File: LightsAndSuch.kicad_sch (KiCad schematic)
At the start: 62 parts, among them J1 Conn_ARM_SWD_TagConnect_TC2030, Q1 AO3400A, Q2 AO3400A, Q3 AO3400A, U1 STM32F205RBTx, U2 MAX98357A, U3 TPS54202DDC, U4 TPS7A20xxxDQN, U5 CD4081BM, U6 LM555xM, U7 LM555xM

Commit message: more or less finished with power
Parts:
- removed U4: TPS7A20xxxDQN, Package_SON:Texas_X2SON-4_1x1mm_P0.65mm, symbol Regulator_Linear:TPS7A20xxxDQN
- added J2: VIN, Connector_Molex:Molex_Micro-Fit_3.0_43045-0200_2x01_P3.00mm_Horizontal, symbol Connector:Conn_01x02_Pin
- added J3: TSA, Connector_Molex:Molex_Micro-Fit_3.0_43045-0200_2x01_P3.00mm_Horizontal, symbol Connector:Conn_01x02_Pin
- added J4: BMS Fault, Connector_Molex:Molex_Micro-Fit_3.0_43045-0200_2x01_P3.00mm_Horizontal, symbol Connector:Conn_01x02_Pin
- added J5: Button, Connector_Molex:Molex_Micro-Fit_3.0_43045-0200_2x01_P3.00mm_Horizontal, symbol Connector:Conn_01x02_Pin
- added J6: IMD Fault, Connector_Molex:Molex_Micro-Fit_3.0_43045-0200_2x01_P3.00mm_Horizontal, symbol Connector:Conn_01x02_Pin
- added J7: Break, Connector_Molex:Molex_Micro-Fit_3.0_43045-0200_2x01_P3.00mm_Horizontal, symbol Connector:Conn_01x02_Pin
- added U4: PTPS7A20185PDQNR, PTPS7A20185PDQNR:DQN0004A-MFG, symbol PTPS7A20185PDQNR:PTPS7A20185PDQNR
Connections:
- net +12V: now also J2.2 (Pin_2)
- net +3.3V: now also U4.1 (OUT)
- net +5V: now also U4.3 (EN), U4.4 (IN)
- net BMS_Fault: now also J4.2 (Pin_2)
- net Break: now also J7.2 (Pin_2)
- net Button: now also J5.2 (Pin_2)
- net GND: now also J2.1 (Pin_1), J3.1 (Pin_1), J4.1 (Pin_1), J5.1 (Pin_1), J6.1 (Pin_1), J7.1 (Pin_1), U4.2 (GND), U4.5 (Thermal_Pad)
- net IMD_Fault: now also J6.2 (Pin_2)
- net TSA: now also J3.2 (Pin_2)
- net SW: now reaches Cboot1.2, L1.1, U3.2 (SW)
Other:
- note added: "Connectors"
- moved on the sheet: C7, C8

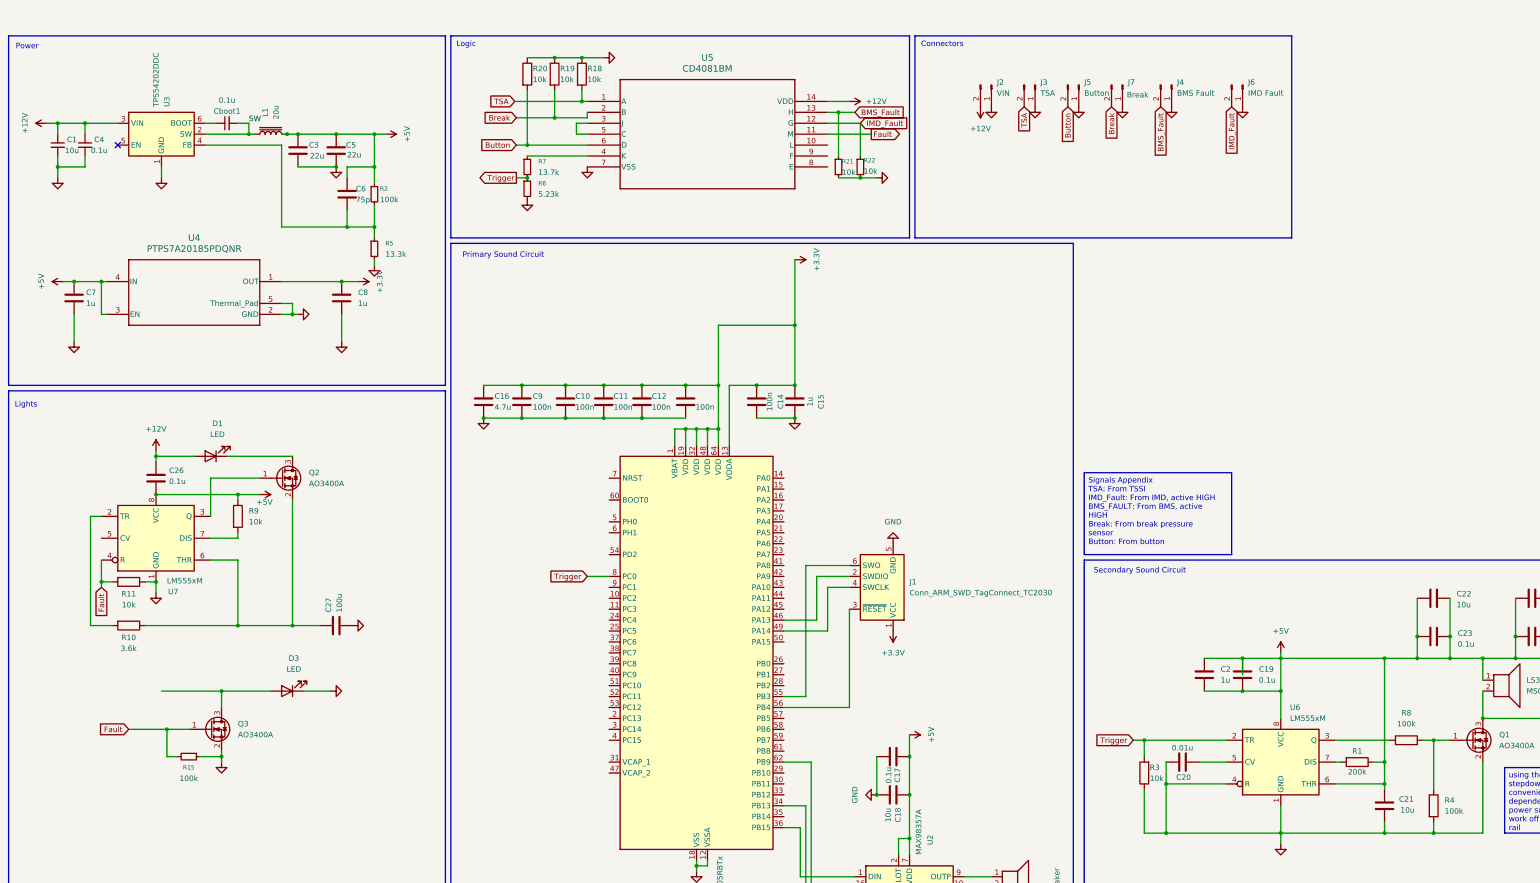
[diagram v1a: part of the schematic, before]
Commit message: finished power layout + inverted sig
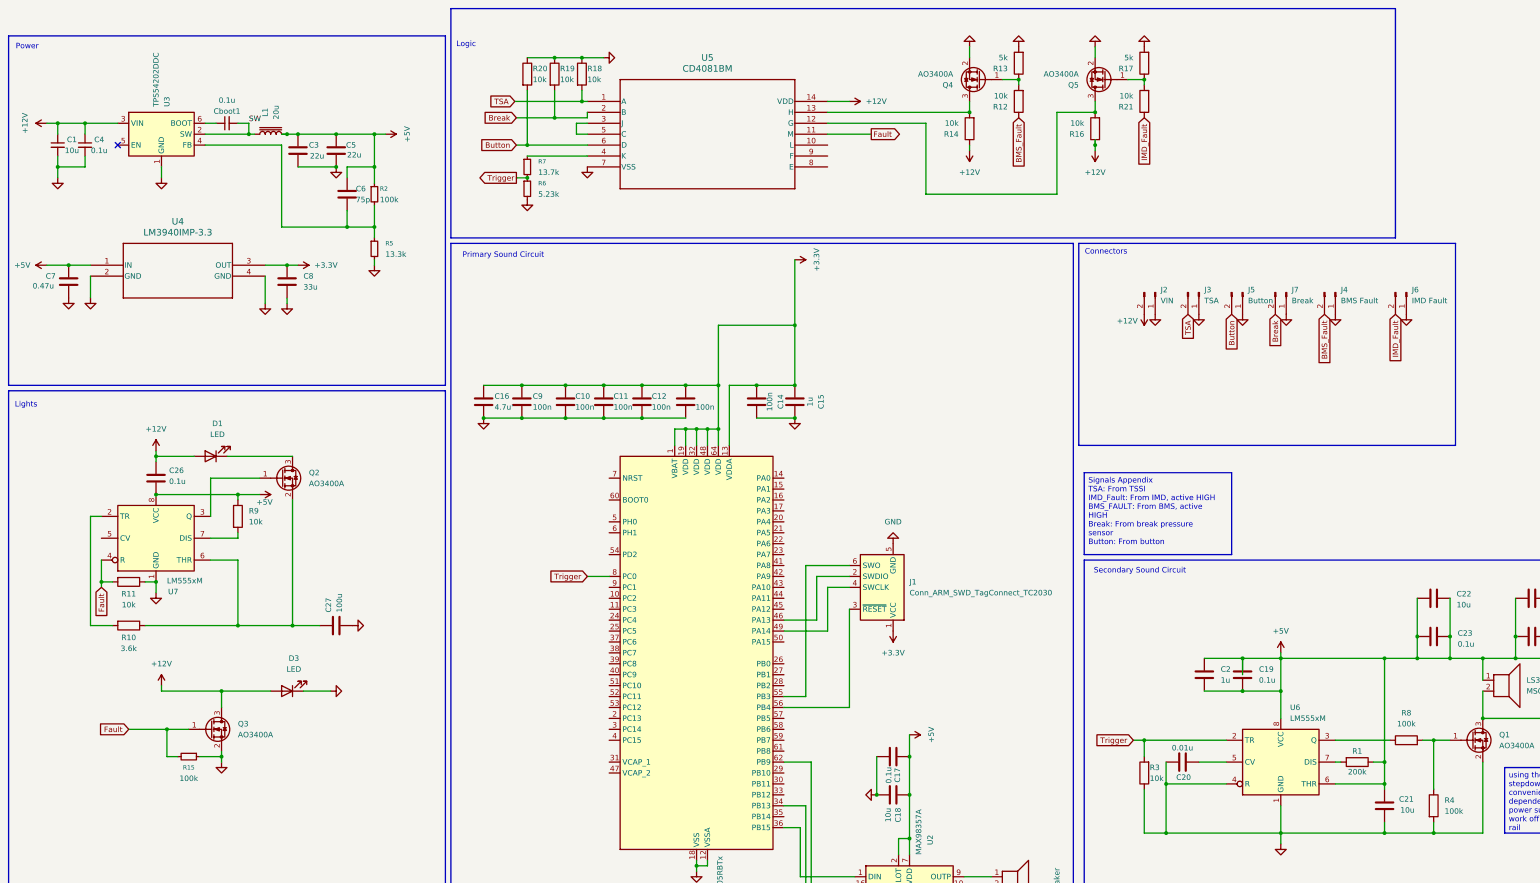
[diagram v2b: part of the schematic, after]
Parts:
- removed R21, R22: 10k, Resistor_SMD:R_0603_1608Metric, symbol Device:R_Small
- removed U4: PTPS7A20185PDQNR, PTPS7A20185PDQNR:DQN0004A-MFG, symbol PTPS7A20185PDQNR:PTPS7A20185PDQNR
- added Q4, Q5: AO3400A, Package_TO_SOT_SMD:SOT-23, symbol Transistor_FET:AO3400A
- added R12, R14, R16, R21: 10k, Resistor_SMD:R_0603_1608Metric, symbol Device:R
- added R13, R17: 5k, Resistor_SMD:R_0603_1608Metric, symbol Device:R
- added U4: LM3940IMP-3.3, LM3940:MP04A, symbol LM3940:LM3940IMP-3.3
- C7: value 1u -> 0.47u; footprint Capacitor_SMD:C_0201_0603Metric -> Capacitor_SMD:C_0603_1608Metric
- C8: value 1u -> 33u; footprint Capacitor_SMD:C_0201_0603Metric -> Capacitor_SMD:C_0603_1608Metric
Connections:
- net +12V: now also D3.2 (A), Q3.3 (D), R14.1, R16.1
- net +3.3V: now also U4.3 (OUT)
- net +5V: now also U4.1 (IN)
- net BMS_Fault: now also R12.1; no longer U5.13 (H)
- net GND: now also Q4.2 (S), Q5.2 (S), R13.2, R17.2, U4.2 (GND), U4.4 (GND)
- net IMD_Fault: now also R21.1; no longer U5.12 (G)
- new net: Q5.3 (D), R16.2, U5.12 (G)
- new net: Q5.1 (G), R17.1, R21.2
- new net: Q4.3 (D), R14.2, U5.13 (H)
- new net: Q4.1 (G), R12.2, R13.1
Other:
- moved on the sheet: J2, J3, J4, J5, J6, J7

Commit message: rp2040
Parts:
- removed J1: Conn_ARM_SWD_TagConnect_TC2030, Connector:Tag-Connect_TC2030-IDC-FP_2x03_P1.27mm_Vertical, symbol Connector:Conn_ARM_SWD_TagConnect_TC2030
- removed U1: STM32F205RBTx, Package_QFP:LQFP-64_10x10mm_P0.5mm, symbol MCU_ST_STM32F2:STM32F205RBTx
- added C28, C29, C30: C, Capacitor_SMD:C_0201_0603Metric, symbol Device:C
- added C31: 100n, Capacitor_SMD:C_0201_0603Metric, symbol Device:C
- added C32, C33: 10u, Capacitor_SMD:C_0201_0603Metric, symbol Device:C
- added J1: Conn_01x02_Pin, Connector_PinHeader_2.00mm:PinHeader_1x02_P2.00mm_Vertical, symbol Connector:Conn_01x02_Pin
- added P1: USB_C_Plug_USB2.0, Connector_USB:USB_C_Receptacle_Amphenol_124019772112A, symbol Connector:USB_C_Plug_USB2.0
- added R22: 1k, Resistor_SMD:R_0603_1608Metric, symbol Device:R
- added U1: RP2040, Package_DFN_QFN:QFN-56-1EP_7x7mm_P0.4mm_EP3.2x3.2mm, symbol MCU_RaspberryPi:RP2040
- added U8: W25Q128JVS, Package_SO:SOIC-8_5.3x5.3mm_P1.27mm, symbol Memory_Flash:W25Q128JVS
- added U9: NCP1117-3.3_SOT223, Package_TO_SOT_SMD:SOT-223-3_TabPin2, symbol Regulator_Linear:NCP1117-3.3_SOT223
- C15: value 1u -> 100n
- C16: value 4.7u' -> 100n
- C9: value 100n -> 1u
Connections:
- net +3.3V: now also C14.1, C15.1, C9.2, C31.1, C32.1, U1.1 (IOVDD), U1.10 (IOVDD), U1.22 (IOVDD), U1.33 (IOVDD), U1.42 (IOVDD), U1.43 (ADC_AVDD), U1.44 (VREG_IN), U1.48 (USB_VDD), U1.49 (IOVDD), U8.8 (VCC), U9.2 (VO); no longer C14.2, C15.2, C9.1
- net GND: now also C14.2, C15.2, C9.1, C28.2, C29.2, C30.2, C31.2, C32.2, C33.2, J1.1 (Pin_1), P1.A1 (GND), P1.A12 (GND), P1.B1 (GND), P1.B12 (GND), P1.S1 (SHIELD), U1.57 (GND), U8.4 (GND), U9.1 (GND); no longer C14.1, C15.1, C9.2
- net Trigger: now also U1.2 (GPIO0)
- net at U2.16 (BCLK): now also U1.14 (GPIO11)
- net at U2.1 (DIN): now also U1.15 (GPIO12)
- net at U2.14 (LRCLK): now also U1.13 (GPIO10)
- new net: C28.1, C29.1, C30.1, U1.23 (DVDD), U1.45 (VREG_VOUT), U1.50 (DVDD)
- new net: C33.1, P1.A4 (VBUS), P1.A9 (VBUS), P1.B4 (VBUS), P1.B9 (VBUS), U9.3 (VI)
- new net: J1.2 (Pin_2), R22.1
- new net QSPI_SCLK: U1.53 (QSPI_SD0), U8.6 (CLK)
- new net QSPI_SD1: U1.54 (QSPI_SD2), U8.2 (DO/IO_{1})
- new net QSPI_SD2: U1.51 (QSPI_SD3), U8.3 (~{WP}/IO_{2})
- new net QSPI_SD3: U1.52 (QSPI_SCLK), U8.7 (~{HOLD}/~{RESET}/IO_{3})
- new net QSPI_SDO: U1.55 (QSPI_SD1), U8.5 (DI/IO_{0})
- new net QSPI_SS: R22.2, U1.56 (QSPI_SS), U8.1 (~{CS})
- new net USB_D+: P1.A7 (D-), U1.47 (USB_DP)
- new net USB_D-: P1.A6 (D+), U1.46 (USB_DM)
- no-connect marks 1 -> 2
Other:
- moved on the sheet: C1, C17, C18, C19, C2, C20, C21, C22, C23, C24, C25, C26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

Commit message: switching out the connectors need to fix net names
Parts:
- removed D1, D3: LED, Connector_Molex:Molex_Micro-Fit_3.0_43045-0200_2x01_P3.00mm_Horizontal, symbol Device:LED
- removed J2: VIN, Connector_Molex:Molex_Micro-Fit_3.0_43045-0200_2x01_P3.00mm_Horizontal, symbol Connector:Conn_01x02_Pin
- removed J3: TSA, Connector_Molex:Molex_Micro-Fit_3.0_43045-0200_2x01_P3.00mm_Horizontal, symbol Connector:Conn_01x02_Pin
- removed J4: BMS Fault, Connector_Molex:Molex_Micro-Fit_3.0_43045-0200_2x01_P3.00mm_Horizontal, symbol Connector:Conn_01x02_Pin
- removed J5: Button, Connector_Molex:Molex_Micro-Fit_3.0_43045-0200_2x01_P3.00mm_Horizontal, symbol Connector:Conn_01x02_Pin
- removed J6: IMD Fault, Connector_Molex:Molex_Micro-Fit_3.0_43045-0200_2x01_P3.00mm_Horizontal, symbol Connector:Conn_01x02_Pin
- removed J7: Break, Connector_Molex:Molex_Micro-Fit_3.0_43045-0200_2x01_P3.00mm_Horizontal, symbol Connector:Conn_01x02_Pin
- removed LS1: Speaker, Connector_Molex:Molex_Micro-Fit_3.0_43045-0200_2x01_P3.00mm_Horizontal, symbol Device:Speaker
- removed LS2, LS3: MSO206NR, Connector_Molex:Molex_Micro-Fit_3.0_43045-0200_2x01_P3.00mm_Horizontal, symbol Device:Speaker
- added FB1: FerriteBead, symbol Device:FerriteBead
- added J2, J8: Conn_02x06_Odd_Even, Connector_Hirose:Hirose_DF11-12DP-2DSA_2x06_P2.00mm_Vertical, symbol Connector_Generic:Conn_02x06_Odd_Even
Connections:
- net +12V: now also FB1.2, J2.7 (Pin_7), J2.9 (Pin_9)
- net +5V: now also J2.3 (Pin_3), J2.5 (Pin_5)
- net BMS_Fault: now also J8.8 (Pin_8)
- net Break: now also J8.6 (Pin_6)
- net Button: now also J8.4 (Pin_4)
- net GND: now also J2.8 (Pin_8), J8.1 (Pin_1), J8.11 (Pin_11), J8.3 (Pin_3), J8.5 (Pin_5), J8.7 (Pin_7), J8.9 (Pin_9)
- net IMD_Fault: now also J8.2 (Pin_2)
- net TSA: now also J8.10 (Pin_10)
- net FAULT_CATHODE: now reaches Q2.3 (D)
- net FAULT_CATHODE: now also J2.10 (Pin_10)
- net LS2_n: now reaches Q1.3 (D)
- net LS2_n: now also J2.4 (Pin_4), J2.6 (Pin_6)
- net LS1_P: now reaches U2.9 (OUTP)
- net LS1_P: now also J2.1 (Pin_1)
- net LS1_N: now reaches U2.10 (OUTN)
- net LS1_N: now also J2.2 (Pin_2)
- new net VIN: FB1.1, J8.12 (Pin_12)
- no-connect marks 2 -> 5

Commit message: changed from global labels to net labels
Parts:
- removed FB1: FerriteBead, symbol Device:FerriteBead
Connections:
- net +12V: now also J2.1 (Pin_1), J2.5 (Pin_5); no longer J2.7 (Pin_7), J2.9 (Pin_9)
- net +5V: now also J2.7 (Pin_7); no longer J2.5 (Pin_5)
- net GND: now also J2.6 (Pin_6); no longer J2.8 (Pin_8)
- net LS1_N: now also J2.10 (Pin_10); no longer J2.2 (Pin_2)
- net LS1_P: now also J2.9 (Pin_9); no longer J2.1 (Pin_1)
- net FAULT_CATHODE renamed FAULT_N
- net FAULT_N: now also J2.2 (Pin_2); no longer J2.10 (Pin_10)
- net LS2_n renamed LS2_N
- net LS2_N: now also J2.8 (Pin_8); no longer J2.6 (Pin_6)

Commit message: some updates
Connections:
- net IMD_Fault: now also J8.12 (Pin_12); no longer J8.2 (Pin_2)
- net VIN: now also J8.2 (Pin_2); no longer J8.12 (Pin_12)
- no-connect marks 5 -> 3
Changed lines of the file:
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@@
-	)
-	(no_connect
-		(at 284.48 120.65)
-	)
-	(no_connect
-		(at 163.83 96.52)
 	)
 	(no_connect
@@
 		(at 368.3 125.73)
 	)
-	(bus_entry
-		(at 166.37 212.09)
-		(size 2.54 2.54)
-		(stroke
-			(width 0)
-			(type default)
-		)
-	)
 	(wire
 		(pts
@@
 		(pts
 			(xy 115.57 34.29) (xy 115.57 43.18)
-		)
-		(stroke
-			(width 0)
-			(type default)
-		)
-	)
-	(wire
-		(pts
-			(xy 330.2 125.73) (xy 330.2 124.46)
 		)
 		(stroke
@@
 		)
 	)
-	(label "VIN"
-		(at 330.2 125.73 0)
-		(effects
-			(font
-				(size 1.27 1.27)
-			)
-			(justify left bottom)
-		)
-	)
 	(label "QSPI_SD2"
 		(at 179.07 173.99 0)
+		(effects
+			(font
+				(size 1.27 1.27)
+			)
+			(justify left bottom)
+		)
+	)
+	(label "VIN"
+		(at 330.2 111.76 0)
 		(effects
 			(font
@@
 		)
 	)
-	(global_label "IMD_Fault"
-		(shape input)
-		(at 330.2 111.76 0)
-		(fields_autoplaced yes)
-		(effects
-			(font
-				(size 1.27 1.27)
-			)
-			(justify left)
-		)
-		(property "Intersheetrefs" "${INTERSHEET_REFS}"
-			(at 342.2565 111.76 0)
-			(effects
-				(font
-					(size 1.27 1.27)
-				)
-				(justify left)
-				(hide yes)
-			)
-		)
-	)
 	(global_label "Trigger"
 		(shape output)
@@
 				(hide yes)
 			)
+		)
+	)
+	(global_label "IMD_Fault"
+		(shape input)
+		(at 330.2 124.46 0)
+		(fields_autoplaced yes)
+		(effects
+			(font
+				(size 1.27 1.27)
+			)
+			(justify left)
+		)
+		(property "Intersheetrefs" "${INTERSHEET_REFS}"
+			(at 342.2565 124.46 0)
+			(effects
+				(font
+					(size 1.27 1.27)
+				)
+				(justify left)
+				(hide yes)
+			)

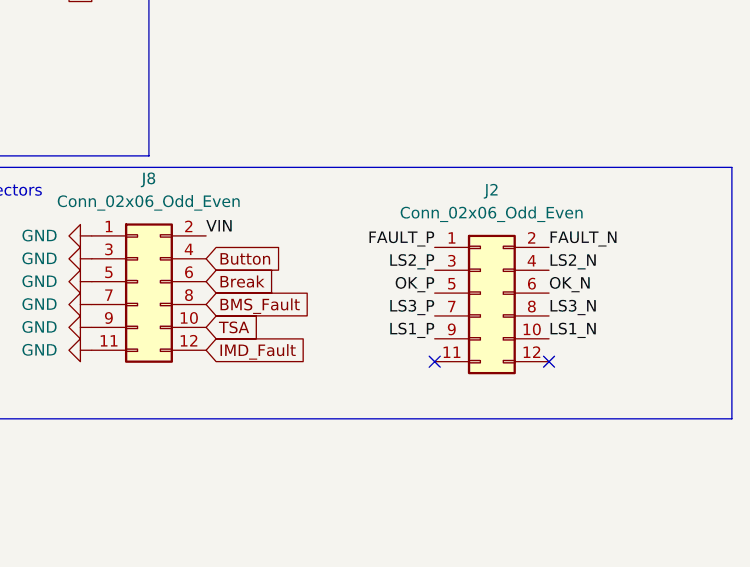
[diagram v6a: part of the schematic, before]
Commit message: some decoup caps
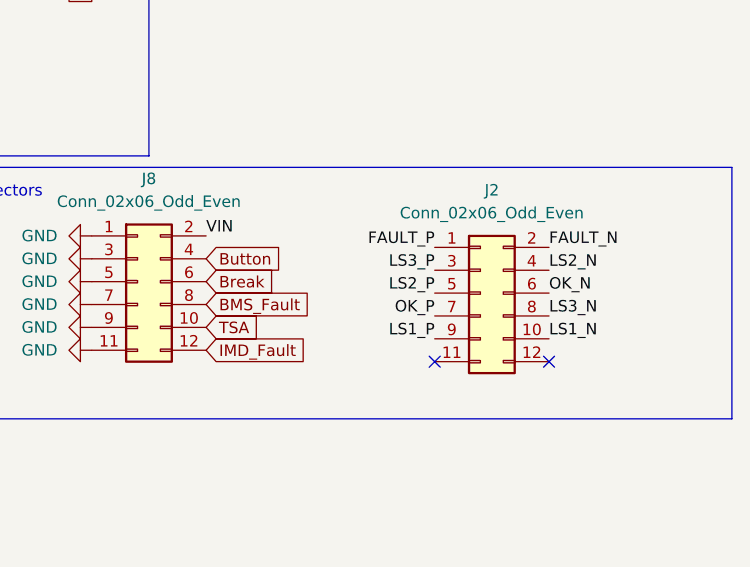
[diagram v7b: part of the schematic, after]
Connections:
- net +12V: now also J2.7 (Pin_7); no longer J2.5 (Pin_5)
- net +5V: now also J2.5 (Pin_5); no longer J2.7 (Pin_7)
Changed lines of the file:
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@@
+		)
+	)
+	(label "LS2_P"
+		(at 355.6 118.11 180)
+		(effects
+			(font
+				(size 1.27 1.27)
+			)
+			(justify right bottom)
 		)
 	)
@@
 		)
 	)
-	(label "LS2_P"
-		(at 355.6 115.57 180)
-		(effects
-			(font
-				(size 1.27 1.27)
-			)
-			(justify right bottom)
-		)
-	)
 	(label "USB_D-"
 		(at 177.8 153.67 0)
@@
 		)
 	)
-	(label "OK_P"
-		(at 355.6 118.11 180)
-		(effects
-			(font
-				(size 1.27 1.27)
-			)
-			(justify right bottom)
-		)
-	)
-	(label "LS3_P"
-		(at 355.6 120.65 180)
-		(effects
-			(font
-				(size 1.27 1.27)
-			)
-			(justify right bottom)
-		)
-	)
 	(label "QSPI_SCLK"
 		(at 223.52 250.19 0)
@@
 		)
 	)
+	(label "OK_P"
+		(at 355.6 120.65 180)
+		(effects
+			(font
+				(size 1.27 1.27)
+			)
+			(justify right bottom)
+		)
+	)
 	(label "LS1_N"
 		(at 368.3 123.19 0)
@@
 		)
 	)
+	(label "LS3_P"
+		(at 355.6 115.57 180)
+		(effects
+			(font
+				(size 1.27 1.27)
+			)
+			(justify right bottom)
+		)
+	)

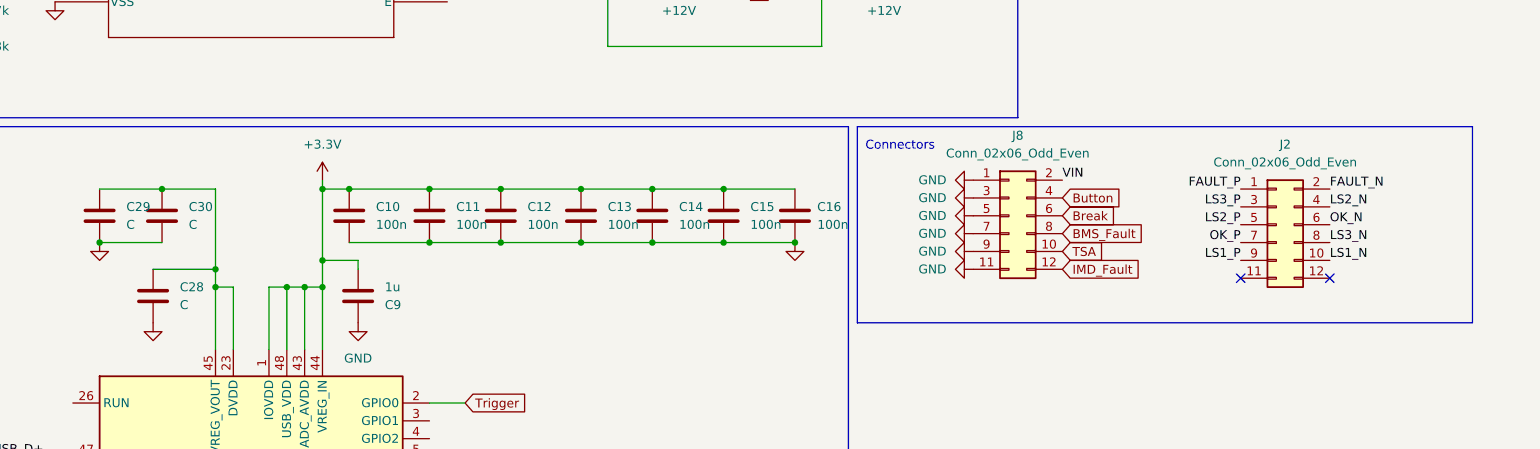
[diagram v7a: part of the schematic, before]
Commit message: passing DRC
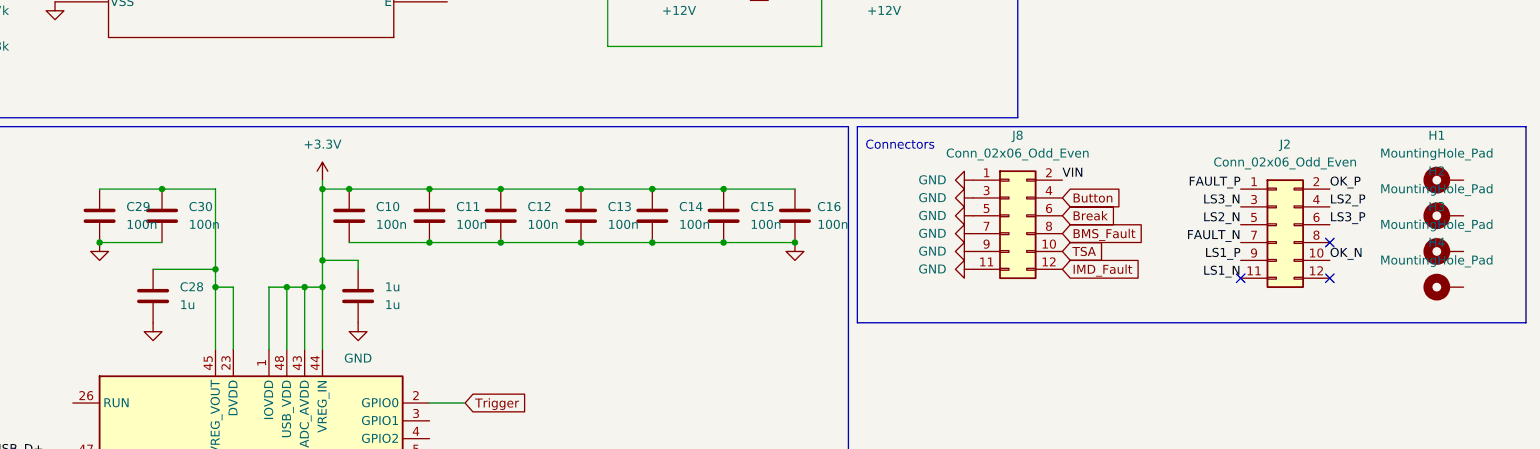
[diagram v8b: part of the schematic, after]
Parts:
- added H1, H2, H3, H4: MountingHole_Pad, MountingHole:MountingHole_4.3mm_M4_DIN965_Pad, symbol Mechanical:MountingHole_Pad
- C28: value C -> 1u
- C29, C30: value C -> 100n
- renumbered C9 to 1u
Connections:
- net +12V: now also J2.2 (Pin_2); no longer J2.7 (Pin_7)
- net +5V: now also J2.4 (Pin_4), J2.6 (Pin_6); no longer J2.3 (Pin_3), J2.5 (Pin_5)
- net FAULT_N: now also J2.7 (Pin_7); no longer J2.2 (Pin_2)
- net GND: now also J2.10 (Pin_10); no longer J2.6 (Pin_6)
- net LS1_N: now also J2.11 (Pin_11); no longer J2.10 (Pin_10)
- net LS2_N: now also J2.3 (Pin_3), J2.5 (Pin_5); no longer J2.4 (Pin_4), J2.8 (Pin_8)
- no-connect marks 3 -> 4
